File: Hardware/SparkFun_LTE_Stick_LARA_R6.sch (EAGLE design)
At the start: 27 parts, among them IC1 SN74AVC4T774PW, IC2 SN74AVC4T774PW, J1 NANO_SIM, J2 U.FL, J3 U.FL, J7 QWIIC_RIGHT_ANGLE, U1 LARA-R6401, U2 AP7361C-33FGEUDFN-8, U3 PCA9306

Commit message: End of day commit
Extend board length
Start adding passives
Plan more routing
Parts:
- added C1, C2, C3, C4: 47pF, SparkFun-Capacitors:47PF-0603-50V-5%
- added C5, C6: 0.1uF, SparkFun-Capacitors:0.1UF-0603-25V-5%
- added D4: DT1042-04SO-7, SparkFun-DiscreteSemi:TVS_DIODE_ARRAY_4DT1042-04SO-7
- added IC3: SN74AVC4T774PW, SparkFun-IC-Comms:SN74AVC4T774PW
- added JP2: JUMPER-SMT_3_2-NC_TRACE_SILK, SparkFun-Jumpers:JUMPER-SMT_3_2-NC_TRACE_SILK
- added R1, R2: 100k, SparkFun-Resistors:100KOHM-0603-1/10W-1%
- added R3, R4: 2.2k, SparkFun-Resistors:2.2KOHM-0603-1/10W-1%
- J5: device SparkFun-Connectors:CONN_08NO_SILK_DNP -> SparkFun-Connectors:CONN_14NO_SILK
- J6: device SparkFun-Connectors:CONN_08NO_SILK_DNP -> SparkFun-Connectors:CONN_10NO_SILK_PTH_FEMALE
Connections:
- removed net I2C_TXD: U1.I2S_TXD
- removed net I2S_CLK: U1.I2S_CLK
- removed net I2S_RXD: U1.I2S_RXD
- removed net I2S_WA: U1.I2S_WA
- new net I2S_CLK_18: IC3.A3, U1.I2S_CLK
- new net I2S_CLK_33: IC3.B3, J6.7
- new net I2S_RXD_18: IC3.A4, U1.I2S_RXD
- new net I2S_RXD_33: IC3.B4, J6.6
- new net I2S_TXD_18: IC3.A2, U1.I2S_TXD
- new net I2S_TXD_33: IC3.B2, J6.8
- new net I2S_WA_18: IC3.A1, U1.I2S_WA
- new net I2S_WA_33: IC3.B1, J6.9
- new net N$1: C6.1, R2.1, U3.EN, U3.VREF2
- new net N$2: JP2.3, R3.2
- new net N$3: JP2.1, R4.1
- new net N$4: J6.10
- new net VIN: J6.3
- net 1.8V: now also IC3.VCCA, J6.5, R1.2
- net 3.3V: now also IC3.VCCB, J6.4, JP2.2, R2.2
- net 5V: now also J6.2
- net GND: now also C1.2, C2.2, C3.2, C4.2, C5.2, C6.2, D4.2, D4.5, IC3.!OE, IC3.GND, J6.1
- net SCL_33: now also R4.2
- net SDA_33: now also R3.1
- net SIM_CLK: now also C2.1, D4.4
- net SIM_DET: now also R1.1
- net SIM_IO: now also C3.1, D4.6
- net SIM_RST: now also C1.1, D4.3
- net VSIM: now also C4.1, C5.1, D4.1
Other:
- moved on the sheet: D2, D3, E1, E2, J1, J2, J3

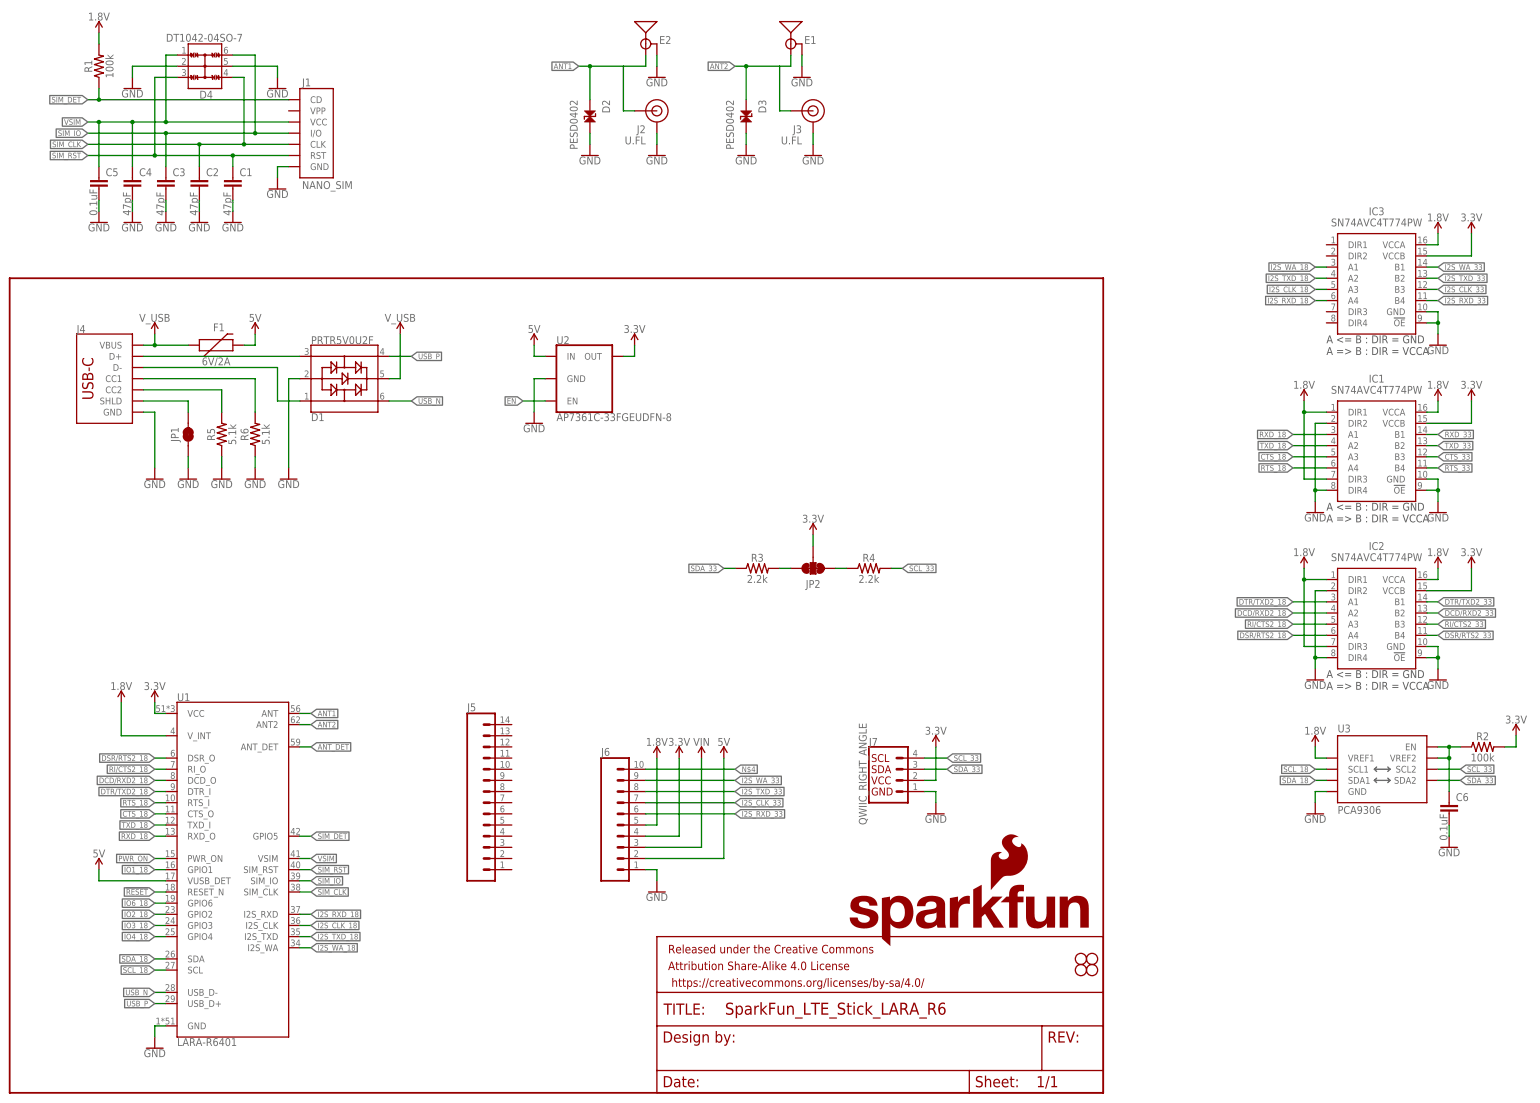
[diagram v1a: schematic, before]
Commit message: Finish initial layout of v01
Change UART2, I2C, and GPIO pins to only be accessible via test points
Shrink board length to 3" again
Set initial header pinouts
Add decoupling capacitors
Route all air wires
Route USB and RF traces with proper impedance
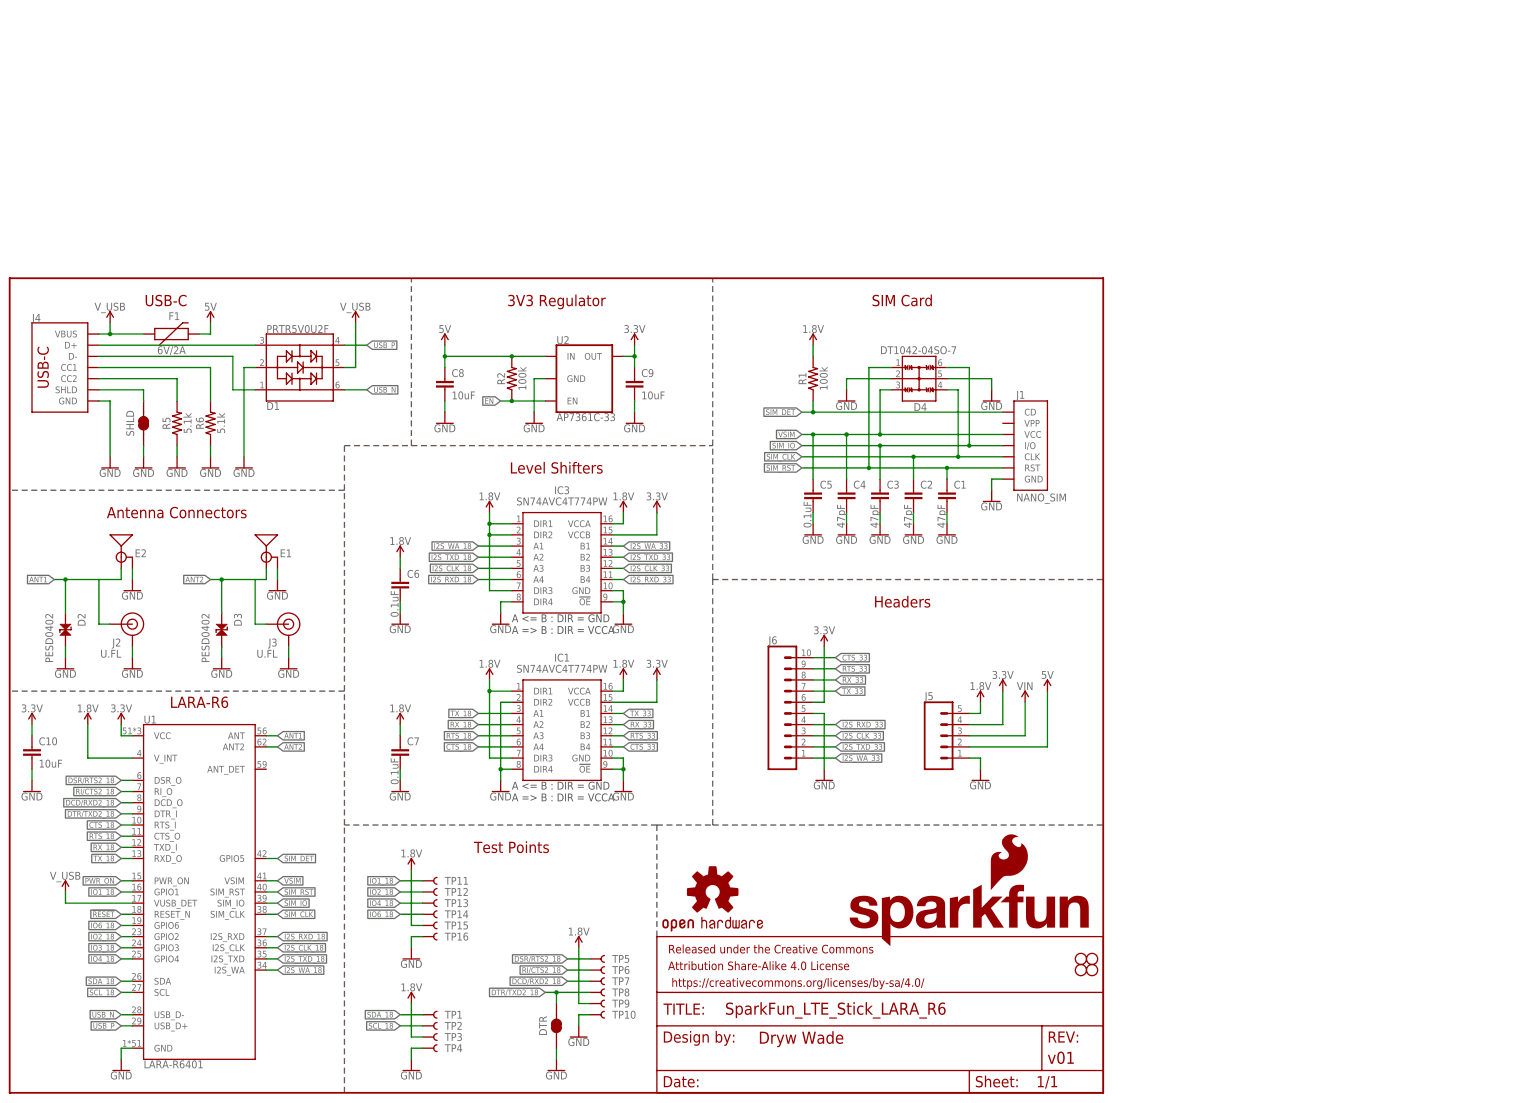
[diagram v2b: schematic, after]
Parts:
- removed IC2: SN74AVC4T774PW, SparkFun-IC-Comms:SN74AVC4T774PW
- removed J7: QWIIC_RIGHT_ANGLE, SparkFun-Connectors:QWIIC_CONNECTORJS-1MM
- removed JP1: JUMPER-SMT_2_NC_TRACE_SILK, SparkFun-Jumpers:JUMPER-SMT_2_NC_TRACE_SILK
- removed JP2: JUMPER-SMT_3_2-NC_TRACE_SILK, SparkFun-Jumpers:JUMPER-SMT_3_2-NC_TRACE_SILK
- removed R3, R4: 2.2k, SparkFun-Resistors:2.2KOHM-0603-1/10W-1%
- removed U3: PCA9306, SparkFun-IC-Comms:PCA9306PCA9306DC
- added C10, C8, C9: 10uF, SparkFun-Capacitors:10UF-0805-25V-10%
- added C7: 0.1uF, SparkFun-Capacitors:0.1UF-0603-25V-5%
- added DTR, SHLD: JUMPER-SMT_2_NC_TRACE_SILK, SparkFun-Jumpers:JUMPER-SMT_2_NC_TRACE_SILK
- added LOGO2: OSHW-LOGOM, SparkFun-Aesthetics:OSHW-LOGOM
- added TP1, TP10, TP11, TP12, TP13, TP14, TP15, TP16, TP2, TP3, TP4, TP5, TP6, TP7, TP8, TP9: TEST-POINT3X5, SparkFun-Connectors:TEST-POINT3X5
- FRAME1: DESIGNER (none) -> Dryw Wade; REV (none) -> v01
- J5: device SparkFun-Connectors:CONN_14NO_SILK -> SparkFun-Connectors:CONN_05NO_SILK
- U2: value AP7361C-33FGEUDFN-8 -> AP7361C-33
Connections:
- net RXD_18 renamed TX_18
- net TXD_18 renamed RX_18
- removed net ANT_DET: U1.ANT_DET
- removed net DCD/RXD2_33: IC2.B2
- removed net DSR/RTS2_33: IC2.B4
- removed net DTR/TXD2_33: IC2.B1
- removed net N$1: C6.1, R2.1, U3.EN, U3.VREF2
- removed net N$2: JP2.3, R3.2
- removed net N$3: JP2.1, R4.1
- removed net N$4: J6.10
- removed net N$7: J4.SHLD, JP1.2
- removed net RI/CTS2_33: IC2.B3
- removed net RXD_33: IC1.B1
- removed net SCL_33: J7.4, R4.2, U3.SCL2
- removed net SDA_33: J7.3, R3.1, U3.SDA2
- removed net TXD_33: IC1.B2
- new net RX_33: IC1.B2, J6.8
- new net SHLD: J4.SHLD, SHLD.2
- new net TX_33: IC1.B1, J6.7
- net 1.8V: now also C6.1, C7.1, IC3.DIR1, IC3.DIR2, IC3.DIR3, J5.5, TP15.1, TP3.1, TP9.1; no longer IC2.DIR1, IC2.DIR3, IC2.VCCA, J6.5, U3.VREF1
- net 3.3V: now also C10.1, C9.1, J5.4, J6.6; no longer IC2.VCCB, J6.4, J7.2, JP2.2, R2.2
- net 5V: now also C8.1, J5.2, R2.2; no longer J6.2, U1.VUSB_DET
- net CTS_18: now also IC1.A4, U1.RTS_I; no longer IC1.A3, U1.CTS_O
- net CTS_33: now also IC1.B4, J6.10; no longer IC1.B3
- net DCD/RXD2_18: now also TP7.1; no longer IC2.A2
- net DSR/RTS2_18: now also TP5.1; no longer IC2.A4
- net DTR/TXD2_18: now also DTR.2, TP8.1; no longer IC2.A1
- net EN: now also R2.1
- net GND: now also C10.2, C7.2, C8.2, C9.2, DTR.1, IC3.DIR4, J5.1, J6.5, SHLD.1, TP10.1, TP16.1, TP4.1; no longer IC2.!OE, IC2.DIR2, IC2.DIR4, IC2.GND, J6.1, J7.1, JP1.1, U3.GND
- net I2S_CLK_33: now also J6.3; no longer J6.7
- net I2S_RXD_33: now also J6.4; no longer J6.6
- net I2S_TXD_33: now also J6.2; no longer J6.8
- net I2S_WA_33: now also J6.1; no longer J6.9
- net IO1_18: now also TP11.1
- net IO2_18: now also TP12.1
- net IO4_18: now also TP13.1
- net IO6_18: now also TP14.1
- net RI/CTS2_18: now also TP6.1; no longer IC2.A3
- net RTS_18: now also IC1.A3, U1.CTS_O; no longer IC1.A4, U1.RTS_I
- net RTS_33: now also IC1.B3, J6.9; no longer IC1.B4
- net SCL_18: now also TP2.1; no longer U3.SCL1
- net SDA_18: now also TP1.1; no longer U3.SDA1
- net SIM_RST: now also D4.1; no longer D4.3
- net VIN: now also J5.3; no longer J6.3
- net VSIM: now also D4.3; no longer D4.1
- net V_USB: now also U1.VUSB_DET
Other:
- note added: "3V3 Regulator"
- note added: "Antenna Connectors"
- note added: "Headers"
- note added: "LARA-R6"
- note added: "Level Shifters"
- note added: "SIM Card"
- note added: "Test Points"
- note added: "USB-C"
- moved on the sheet: C1, C2, C3, C4, C5, C6, D1, D2, D3, D4, E1, E2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
